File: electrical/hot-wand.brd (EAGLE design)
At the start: 112 x 72 mm, 182 parts, among them IC1 12V R-78K12-2.0, IC2 3V3 R-78K3.3, Q1 STP19NF20, Q2 IRF510, Q3 BC846B, Q4 SIRS5800DP-T1-GE3, Q5 2N7002K, Q6 DMTH64M2LPDWQ-13, Q7 G3404, SW1 SW-TACT-SIDE, U1 TPS54560DDA, U2 1EDN8511BXUSA1, U3 INA138, U4 LM74700QDBVTQ1, U5 AP53781, U6 SSD1306-4PIN-0.91N-VERT, U7 STM32F030F4P6, Y1 27.12 MHz 10pF

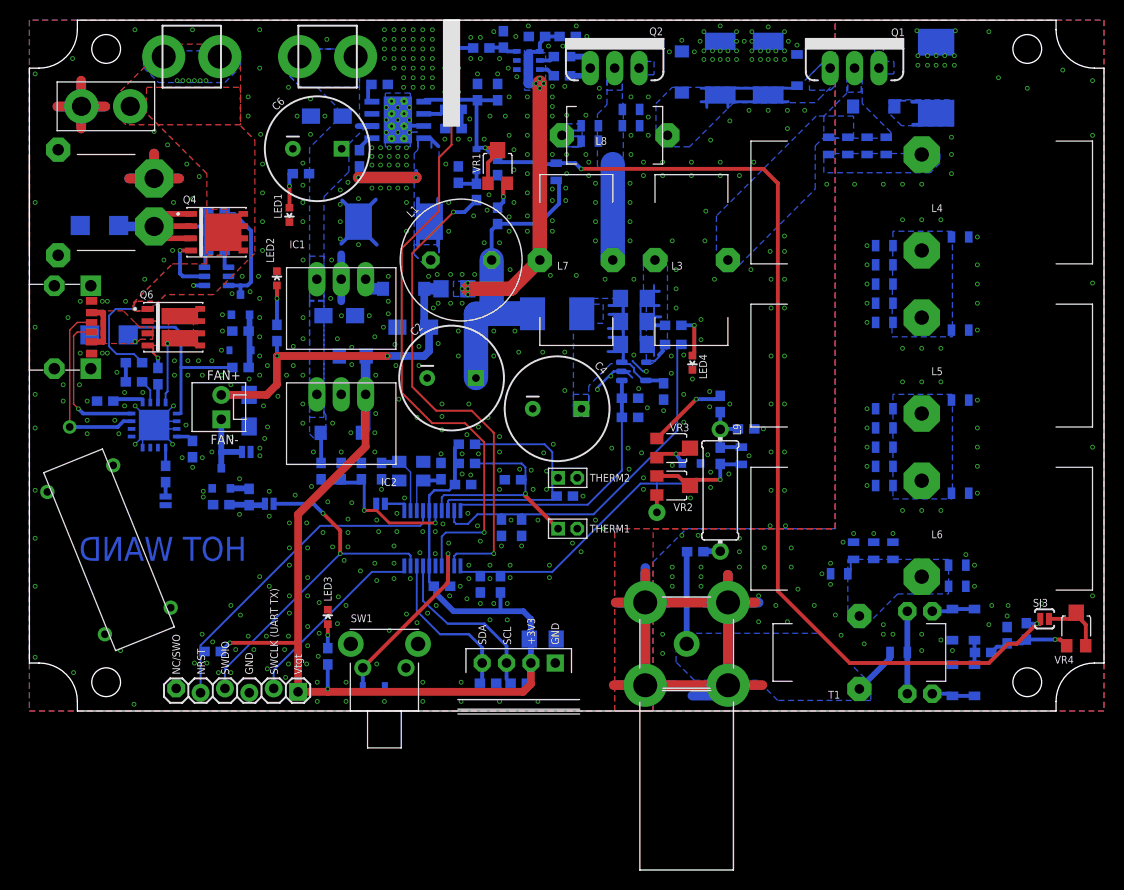
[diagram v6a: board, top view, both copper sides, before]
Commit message: thermal and mech changes
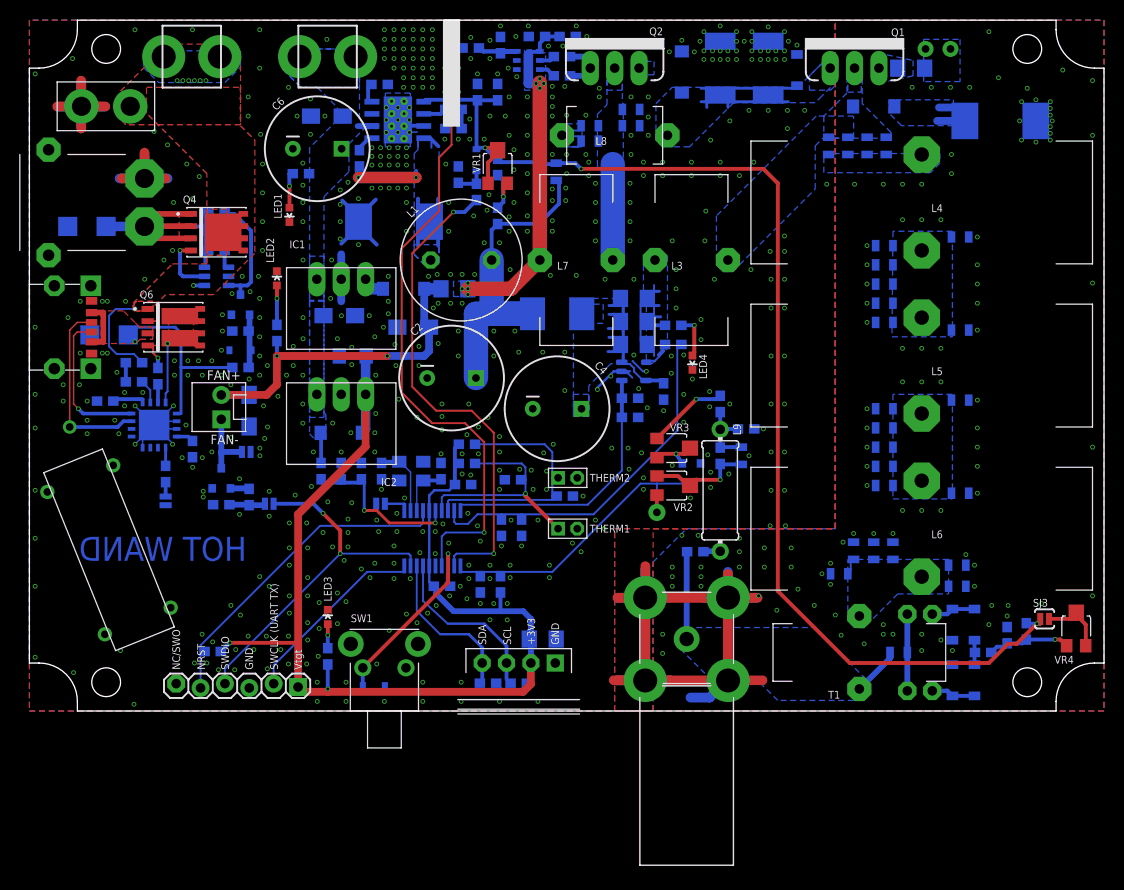
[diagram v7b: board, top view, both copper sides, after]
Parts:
- added R49: (no value), hot-wand:1206
- SW1: value SW-TACT-SIDE -> (none)
- moved TVS1 8.07 mm to (101.2, 61.5), turned to 180 degrees
- moved TVS3 1.30 mm to (6.00, 50.5)
- moved R14 1.10 mm to (46.0, 69.1)
- moved JP3 1.00 mm to (2.00, 53.0)
- moved R16 0.67 mm to (49.1, 69.4)
- moved JP2 0.50 mm to (68.5, 7.50)
- moved JP5 0.50 mm to (28.0, 2.50)
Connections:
- new net N$59: Q1.3, R49.2
- net GND: now also R49.1; no longer Q1.3
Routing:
- net N$7: track 2.70 -> 7.40 mm
- net MCU-RF: track 3.04 -> 6.04 mm
- net N$31: track 29.9 -> 32.8 mm
- net GND: track 162.1 -> 159.9 mm
- net RF-GEN: track 68.1 -> 67.0 mm
- net N$2: track 8.60 -> 8.00 mm
- net SWDIO: track 38.0 -> 37.5 mm
- net RF-OUT: track 14.8 -> 14.3 mm
- net NRST: track 35.1 -> 34.6 mm
- added copper zone on layer 1, net N$31
- added copper zone on layer 16, net N$59

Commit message: added standoffs
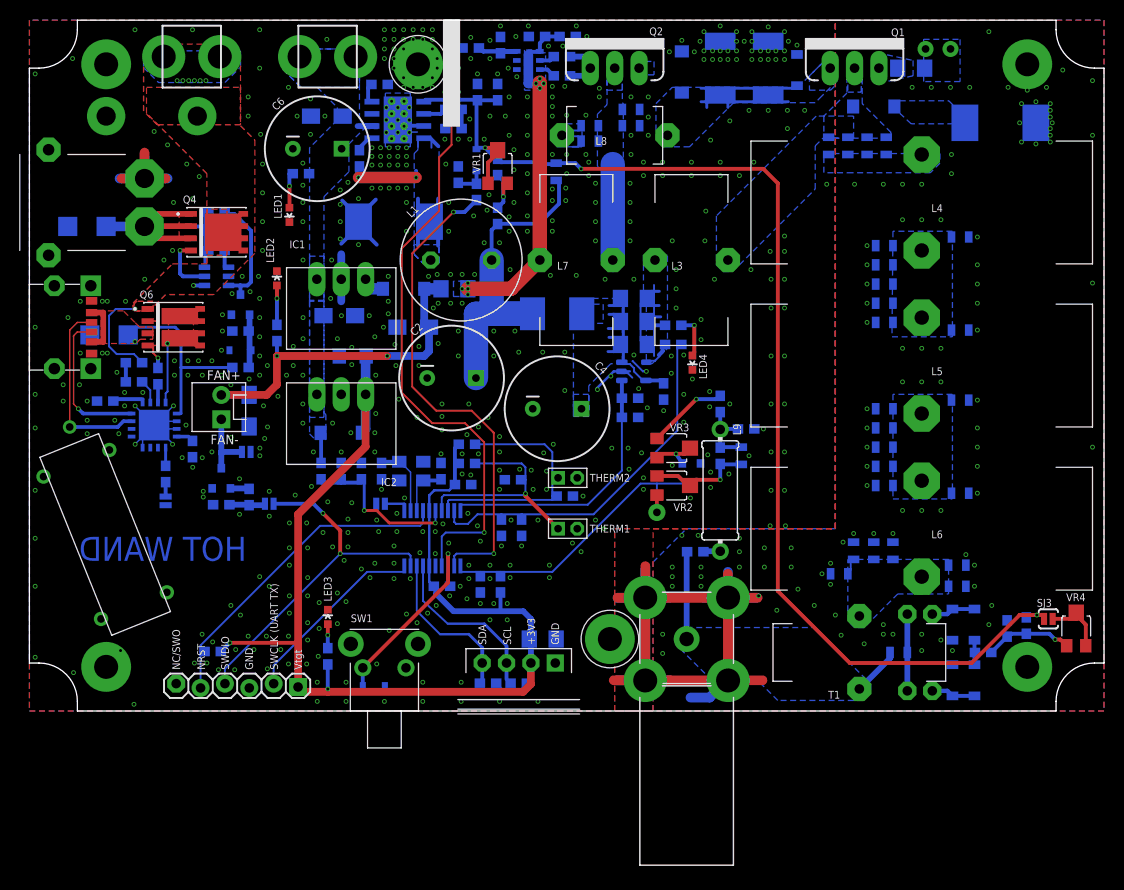
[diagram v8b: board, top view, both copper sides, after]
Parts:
- removed JP5: (no value), hot-wand:1X06_LOCK
- added STANDOFF1, STANDOFF2: STANDOFF-M2.5-4.5MMHEX, hot-wand:STANDOFF-M2.5-4.5MMHEX
- FAN2: value (none) -> FAN-TIEDOWN-20MM-V1
- JP1: value (none) -> COAX-FTYPE-PCB-MNT; device hot-wand:1X02_XTRA_BIG -> hot-wand:CONN_73330-0030_MOL
- JP2: value COAX-FTYPE-PCB-MNT -> USBC-CHGONLY-4M-DRILL; device hot-wand:CONN_73330-0030_MOL -> hot-wand:SAMESKY_UJC-H-G-SMT-2-P6-TR-DRILL
- JP4: value USBC-CHGONLY-4M-DRILL -> (none); device hot-wand:SAMESKY_UJC-H-G-SMT-2-P6-TR-DRILL -> hot-wand:1X06_LOCK
- moved JP1 82.1 mm to (68.5, 7.50), turned to 180 degrees
- moved JP2 73.5 mm to (2.60, 40.0), turned to 270 degrees
- moved JP4 45.3 mm to (28.0, 2.50), turned to 180 degrees
- moved FAN2 1.65 mm to (7.90, 18.4)
- moved C34 0.70 mm to (101.9, 8.60)
- moved R11 0.60 mm to (103.9, 8.90)
- moved SJ3 0.40 mm to (106.2, 9.60)
- moved TVS1 0.20 mm to (101.2, 61.3)
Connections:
- net 3.3V: now also JP4.1; no longer JP5.1
- net DC-SRC: no longer JP1.2
- net GND: now also FAN2.1, FAN2.2, FAN2.3, FAN2.4, JP1.2, JP1.3, JP1.4, JP1.5, JP2.A12, JP2.B12, JP2.M1, JP2.M2, JP2.M3, JP2.M4, JP4.3, PCB1.1, PCB1.2, PCB1.3, PCB1.4, STANDOFF1.1, STANDOFF2.1; no longer JP1.1, JP2.2, JP2.3, JP2.4, JP2.5, JP4.A12, JP4.B12, JP4.M1, JP4.M2, JP4.M3, JP4.M4, JP5.3
- net N$39: now also JP2.A9, JP2.B9; no longer JP4.A9, JP4.B9
- net N$41: now also JP2.B5; no longer JP4.B5
- net N$44: now also JP2.A5; no longer JP4.A5
- net NRST: now also JP4.5; no longer JP5.5
- net RF-OUT: now also JP1.1; no longer JP2.1
- net SWCLK: now also JP4.2; no longer JP5.2
- net SWDIO: now also JP4.4; no longer JP5.4
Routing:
- net GND: track 159.9 -> 140.5 mm, vias 679 -> 667
- net N$7: track 7.40 -> 0.00 mm
- net BUCK-FB: track 128.0 -> 128.9 mm
- net DC-SRC: vias 8 -> 9
